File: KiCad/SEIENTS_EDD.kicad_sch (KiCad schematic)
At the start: 0 parts

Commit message: ArregLATS ERRORS ERC
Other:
- added sheet MÒDUL MAX3232 (MÒDULMAX3232.kicad_sch)
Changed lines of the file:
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@@
+	)
+	(sheet
+		(at 83.82 109.22)
+		(size 64.77 30.48)
+		(exclude_from_sim no)
+		(in_bom yes)
+		(on_board yes)
+		(dnp no)
+		(fields_autoplaced yes)
+		(stroke
+			(width 0.1524)
+			(type solid)
+		)
+		(fill
+			(color 0 0 0 0.0000)
+		)
+		(property "Sheetname" "MÒDUL MAX3232"
+			(at 83.82 108.5084 0)
+			(effects
+				(font
+					(size 1.27 1.27)
+				)
+				(justify left bottom)
+			)
+		)
+		(property "Sheetfile" "MÒDULMAX3232.kicad_sch"
+			(at 83.82 140.2846 0)
+			(effects
+				(font
+					(size 1.27 1.27)
+				)
+				(justify left top)
+			)
+		)
+		(instances
+			(project "SEIENTS_EDD"
+				(path "/b6401b4f-5426-49b8-bb2e-8ecdb19989ef"
+					(page "11")
+				)
+			)
+		)
 	)
 	(sheet

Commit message: Arreglats errors i modificació del microcontrolador
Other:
- note added: "MÒDUL MAX3232"
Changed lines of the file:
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@@
+		)
+	)
+	(text "MÒDUL MAX3232"
+		(exclude_from_sim no)
+		(at 115.57 124.968 0)
+		(effects
+			(font
+				(size 4.064 4.064)
+			)
 		)
 	)

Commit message: Modificació al placement
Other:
- note added: "CALEFACCIÓ"
- note removed: "MOSFET"
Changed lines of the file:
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@@
 		)
 	)
-	(text "MOSFET\n"
+	(text "CALEFACCIÓ"
 		(exclude_from_sim no)
 		(at 48.006 124.206 0)

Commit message: Modificació al placement
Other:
- sheet MOSFET renamed CALEFACCIÓ
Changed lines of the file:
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@@
 			(color 0 0 0 0.0000)
 		)
-		(property "Sheetname" "MOSFET"
+		(property "Sheetname" "CALEFACCIÓ"
 			(at 17.78 107.2384 0)
 			(effects

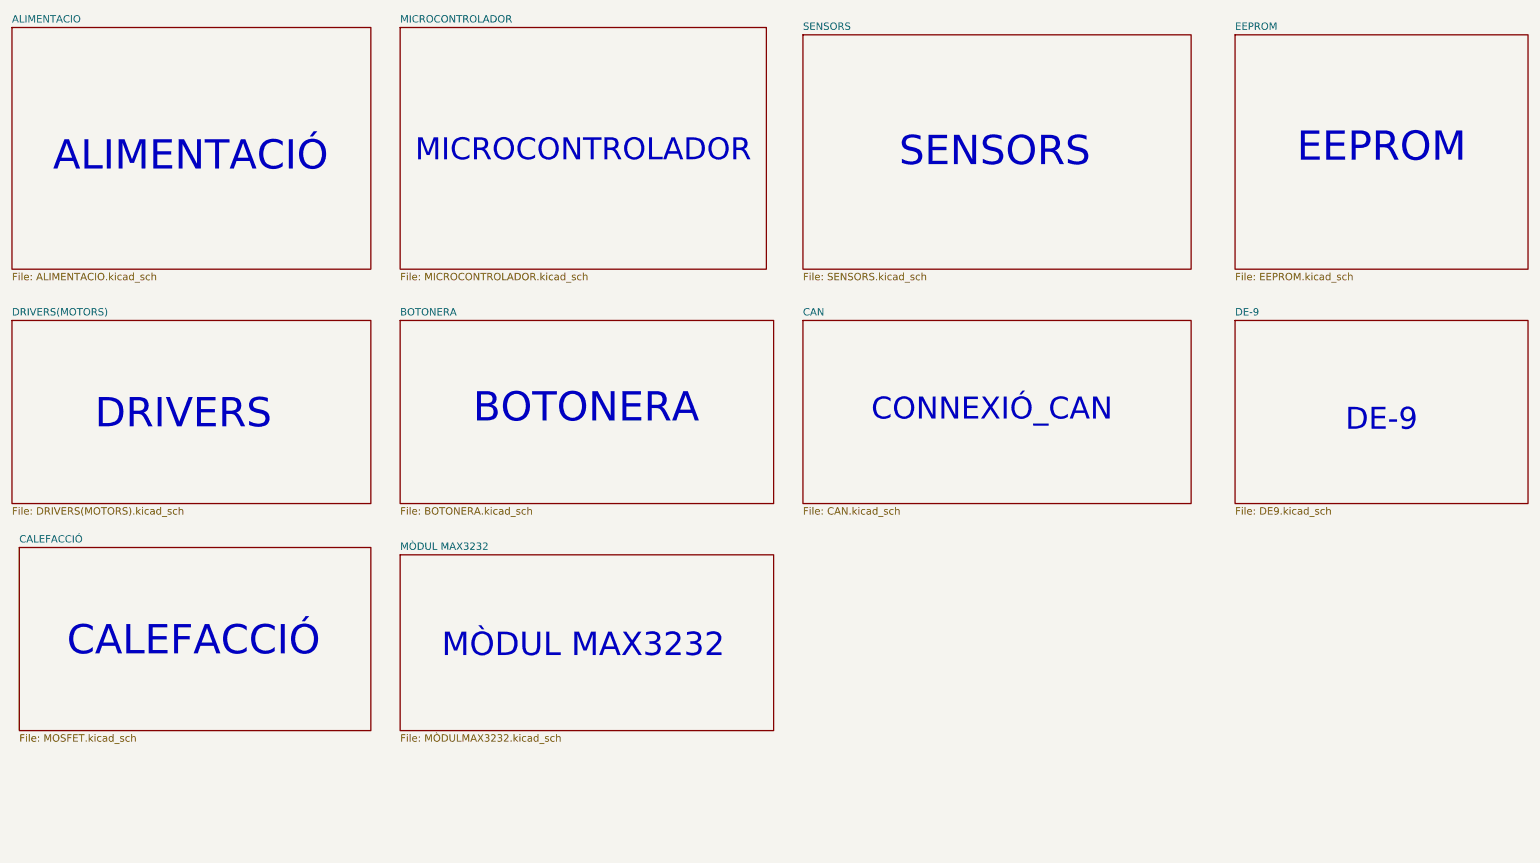
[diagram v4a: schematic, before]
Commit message: Organització Esquematic, asignacio huellas Test Points i Microcontrolador acabat
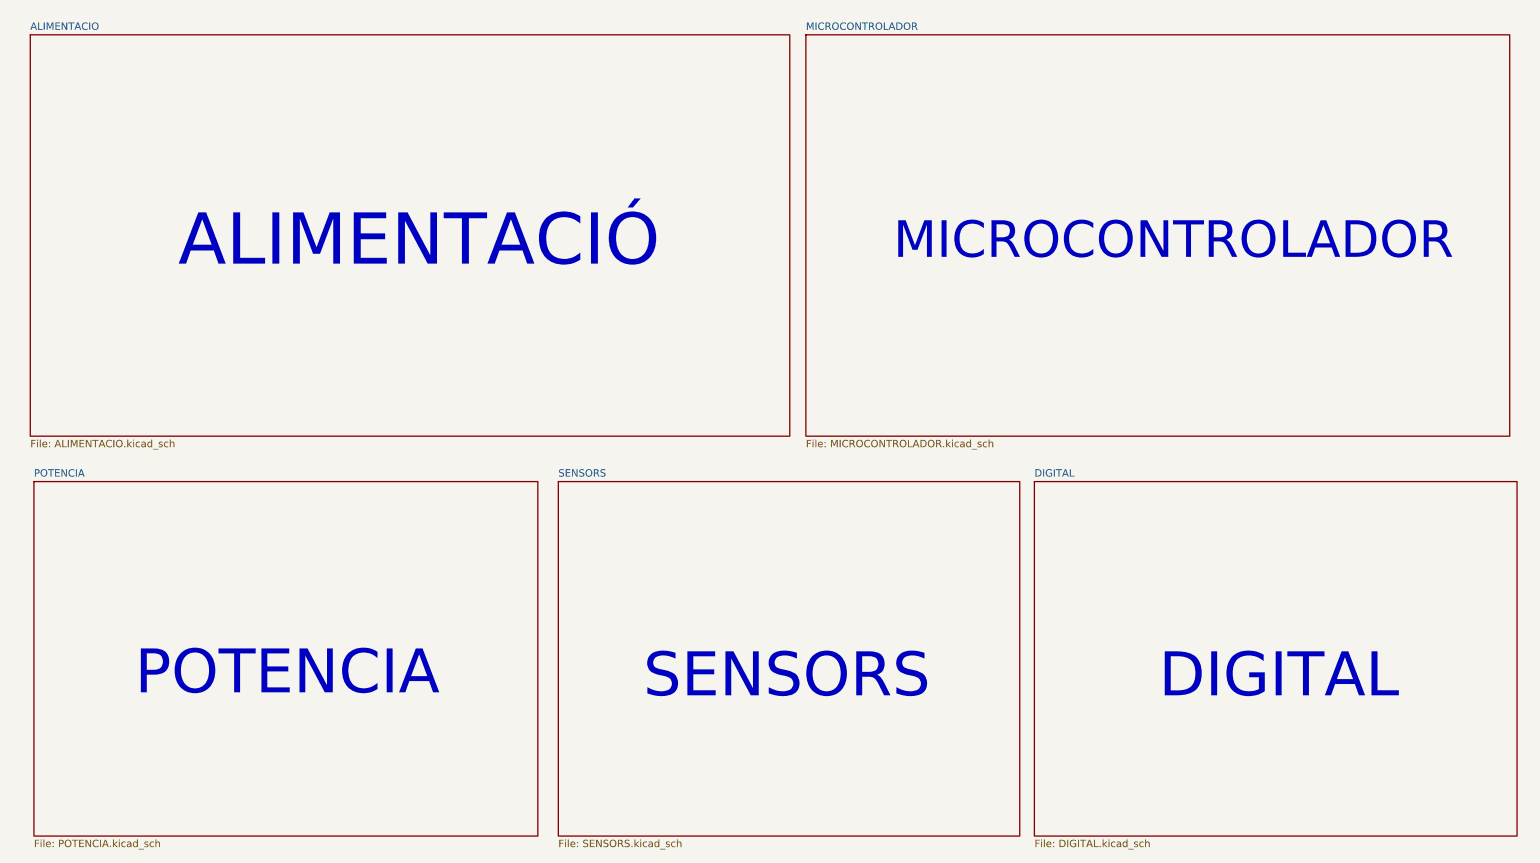
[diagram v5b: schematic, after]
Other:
- removed sheet BOTONERA
- removed sheet CALEFACCIÓ
- removed sheet CAN
- removed sheet DE-9
- removed sheet DRIVERS(MOTORS)
- removed sheet EEPROM
- removed sheet MÒDUL MAX3232
- added sheet DIGITAL (DIGITAL.kicad_sch)
- added sheet POTENCIA (POTENCIA.kicad_sch)
- note added: "DIGITAL"
- note added: "POTENCIA"
- note removed: "BOTONERA"
- note removed: "CALEFACCIÓ"
- note removed: "CONNEXIÓ_CAN"
- note removed: "DE-9"
- note removed: "DRIVERS"
- note removed: "EEPROM"
- note removed: "MÒDUL MAX3232"
